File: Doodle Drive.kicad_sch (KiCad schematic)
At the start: 32 parts, among them J1 USB_B, J2 PINHD_1x4_Male, J6 PINHD_1x2_Male, SW1 Push_Button, SW2 Push_Button, SW3 Push_Button, U1 STM32F411RETx, U6 AP7343-30W5-7, Y1 32.768KHz ±20ppm 12.5pF, Y2 25MHZ 9PF

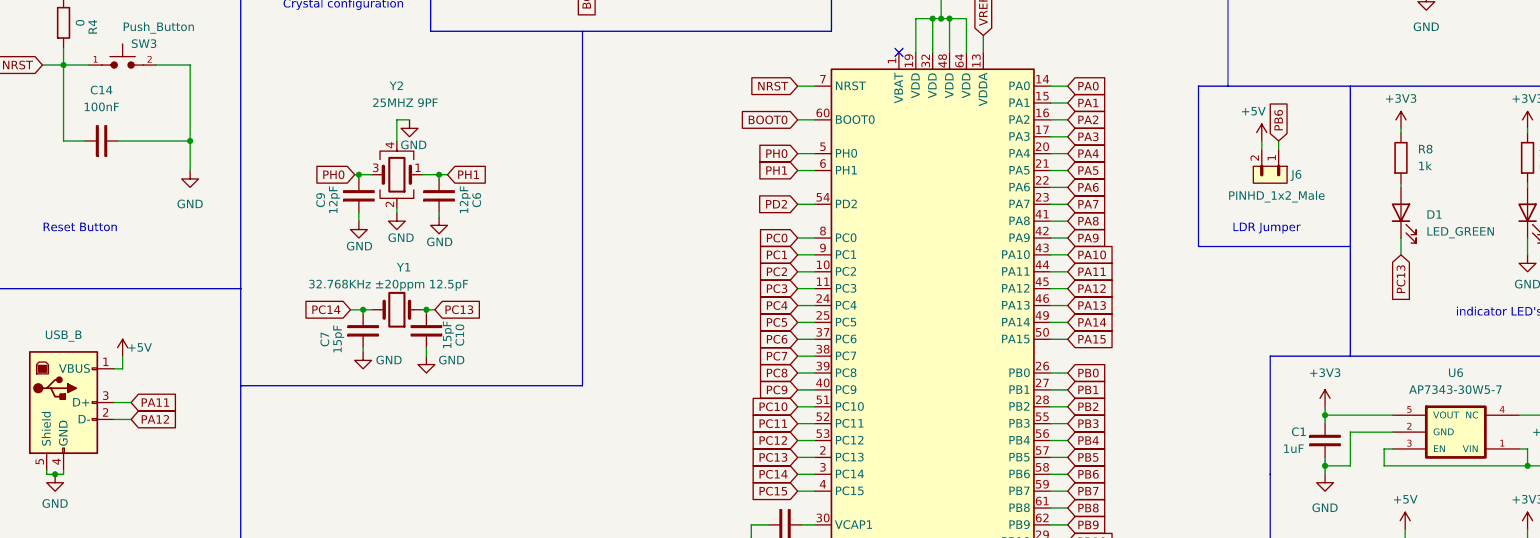
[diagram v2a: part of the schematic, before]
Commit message: fixed few errors, added test points
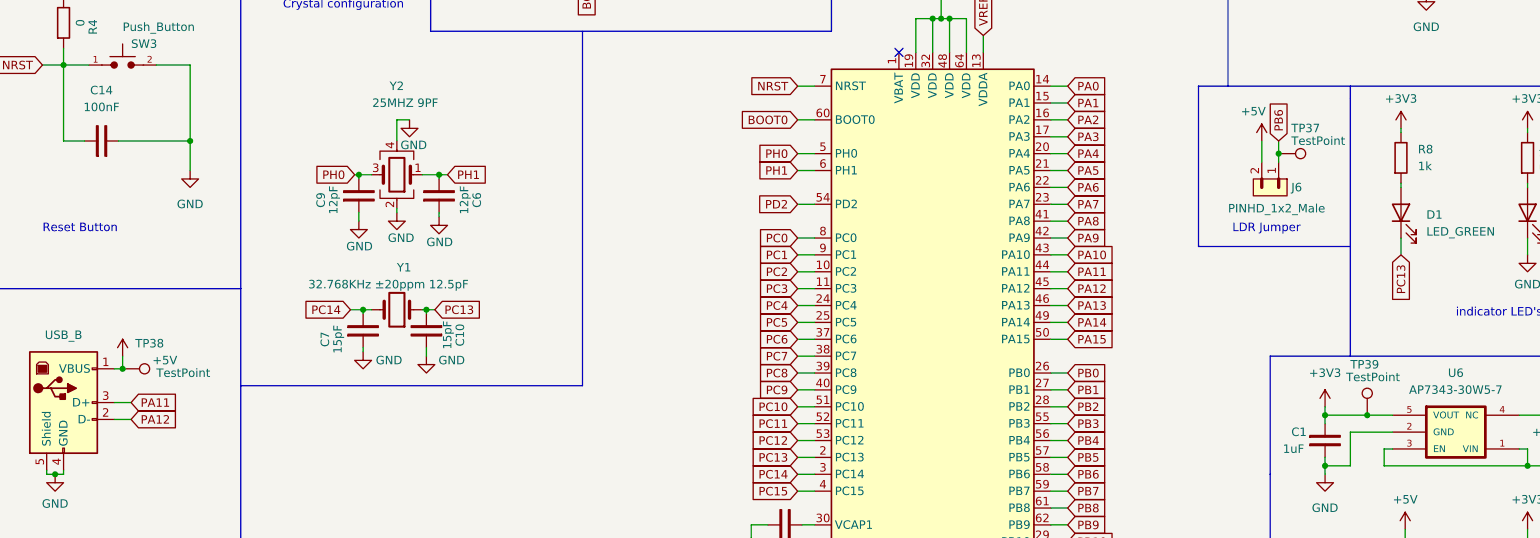
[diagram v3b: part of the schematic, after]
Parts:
- added TP37, TP38, TP39: TestPoint, TestPoint:TestPoint_Pad_D2.5mm, symbol Connector:TestPoint
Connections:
- net +3V3: now also TP39.1
- net +5V: now also TP38.1
- net PB6: now also TP37.1
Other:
- moved on the sheet: J6
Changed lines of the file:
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@@
   (junction (at 227.33 134.62) (diameter 0) (color 0 0 0 0)
   )
+  (junction (at 233.68 127) (diameter 0) (color 0 0 0 0)
+  )
   (junction (at 269.24 50.8) (diameter 0) (color 0 0 0 0)
   )
   (junction (at 36.195 135.89) (diameter 0) (color 0 0 0 0)
   )
+  (junction (at 46.355 120.015) (diameter 0) (color 0 0 0 0)
+  )
   (junction (at 56.515 85.725) (diameter 0) (color 0 0 0 0)
   )
@@
   )
   (junction (at 170.815 67.31) (diameter 0) (color 0 0 0 0)
+  )
+  (junction (at 220.345 87.63) (diameter 0) (color 0 0 0 0)
   )
   (junction (at 255.27 60.96) (diameter 0) (color 0 0 0 0)
@@
     (stroke (width 0) (type default))
   )
-  (wire (pts (xy 220.345 86.995) (xy 220.345 85.725))
+  (wire (pts (xy 220.345 88.9) (xy 220.345 87.63))
     (stroke (width 0) (type default))
   )
@@
     (stroke (width 0) (type default))
   )
+  (wire (pts (xy 233.68 127) (xy 237.49 127))
+    (stroke (width 0) (type default))
+  )
   (wire (pts (xy 256.54 132.08) (xy 257.81 132.08))
     (stroke (width 0) (type default))
@@
     (stroke (width 0) (type default))
   )
-  (wire (pts (xy 227.33 127) (xy 237.49 127))
+  (wire (pts (xy 227.33 127) (xy 233.68 127))
     (stroke (width 0) (type default))
   )
@@
     (stroke (width 0) (type default))
   )
-  (wire (pts (xy 217.805 86.995) (xy 217.805 85.725))
+  (wire (pts (xy 217.805 88.9) (xy 217.805 85.725))
     (stroke (width 0) (type default))
   )
@@
   )
   (wire (pts (xy 168.275 67.31) (xy 168.275 72.39))
+    (stroke (width 0) (type default))
+  )
+  (wire (pts (xy 220.345 87.63) (xy 220.345 85.725))
     (stroke (width 0) (type default))
   )
@@
     )
   )
+  (symbol (lib_id "Connector:TestPoint") (at 233.68 127 0) (unit 1)
+    (in_bom yes) (on_board yes) (dnp no)
+    (property "Reference" "TP39" (at 231.14 119.38 0)
+      (effects (font (size 1.27 1.27)) (justify left))
+    )
+    (property "Value" "TestPoint" (at 230.505 121.285 0)
+      (effects (font (size 1.27 1.27)) (justify left))
+    )
+    (property "Footprint" "TestPoint:TestPoint_Pad_D2.5mm" (at 238.76 127 0)
+      (effects (font (size 1.27 1.27)) hide)
+    )
+    (property "Datasheet" "~" (at 238.76 127 0)
+      (effects (font (size 1.27 1.27)) hide)
+    )
+    (pin "1")
+    (instances
+      (project "Doodle Drive"
+        (path "/3ec634aa-8c09-482d-9325-2288a4dbd68b"
+          (reference "TP39") (unit 1)
+        )
+      )
+    )
+  )
   (symbol (lib_id "PCM_SL_Devices:Capacitor_NP") (at 229.87 55.88 90) (unit 1)
     (in_bom yes) (on_board yes) (dnp no) (fields_autoplaced)
@@
     )
   )
-  (symbol (lib_id "PCM_SL_Pin_Headers:PINHD_1x2_Male") (at 219.075 90.805 270) (unit 1)
+  (symbol (lib_id "PCM_SL_Pin_Headers:PINHD_1x2_Male") (at 219.075 92.71 270) (unit 1)
     (in_bom yes) (on_board yes) (dnp no)
-    (property "Reference" "J6" (at 222.25 90.805 90)
+    (property "Reference" "J6" (at 222.25 92.71 90)
       (effects (font (size 1.27 1.27)) (justify left))
     )
-    (property "Value" "PINHD_1x2_Male" (at 212.725 93.98 90)
+    (property "Value" "PINHD_1x2_Male" (at 212.725 95.885 90)
       (effects (font (size 1.27 1.27)) (justify left))
     )
-    (property "Footprint" "Connector_PinHeader_2.54mm:PinHeader_1x02_P2.54mm_Vertical" (at 215.265 92.075 0)
-      (effects (font (size 1.27 1.27)) hide)
-    )
-    (property "Datasheet" "" (at 226.695 90.805 0)
+    (property "Footprint" "Connector_PinHeader_2.54mm:PinHeader_1x02_P2.54mm_Vertical" (at 215.265 93.98 0)
+      (effects (font (size 1.27 1.27)) hide)
+    )
+    (property "Datasheet" "" (at 226.695 92.71 0)
       (effects (font (size 1.27 1.27)) hide)
     )
@@
       (effects (font (size 1.27 1.27)) hide)
     )
-    (property "Value" "+5V" (at 48.895 116.84 0)
+    (property "Value" "+5V" (at 52.705 118.745 0)
       (effects (font (size 1.27 1.27)))
     )
@@
     )
   )
+  (symbol (lib_id "Connector:TestPoint") (at 46.355 120.015 270) (unit 1)
+    (in_bom yes) (on_board yes) (dnp no)
+    (property "Reference" "TP38" (at 48.26 116.205 90)
+      (effects (font (size 1.27 1.27)) (justify left))
+    )
+    (property "Value" "TestPoint" (at 51.435 120.65 90)
+      (effects (font (size 1.27 1.27)) (justify left))
+    )
+    (property "Footprint" "TestPoint:TestPoint_Pad_D2.5mm" (at 46.355 125.095 0)
+      (effects (font (size 1.27 1.27)) hide)
+    )
+    (property "Datasheet" "~" (at 46.355 125.095 0)
+      (effects (font (size 1.27 1.27)) hide)
+    )
+    (pin "1")
+    (instances
+      (project "Doodle Drive"
+        (path "/3ec634aa-8c09-482d-9325-2288a4dbd68b"
+          (reference "TP38") (unit 1)
+        )
+      )
+    )
+  )
   (symbol (lib_id "power:+5V") (at 261.62 133.35 0) (unit 1)
     (in_bom yes) (on_board yes) (dnp no)
@@
         )
       )
+    )
+  )
+  (symbol (lib_id "Connector:TestPoint") (at 220.345 87.63 270) (unit 1)
+    (in_bom yes) (on_board yes) (dnp no)
+    (property "Reference" "TP37" (at 222.25 83.82 90)
+      (effects (font (size 1.27 1.27)) (justify left))
+    )
+    (property "Value" "TestPoint" (at 222.25 85.725 90)
+      (effects (font (size 1.27 1.27)) (justify left))
+    )
+    (property "Footprint" "TestPoint:TestPoint_Pad_D2.5mm" (at 220.345 92.71 0)
+      (effects (font (size 1.27 1.27)) hide)
+    )
+    (property "Datasheet" "~" (at 220.345 92.71 0)
+      (effects (font (size 1.27 1.27)) hide)
+    )
+    (pin "1")
+    (instances
+      (project "Doodle Drive"
+        (path "/3ec634aa-8c09-482d-9325-2288a4dbd68b"
+          (reference "TP37") (unit 1)
+        )
+      )

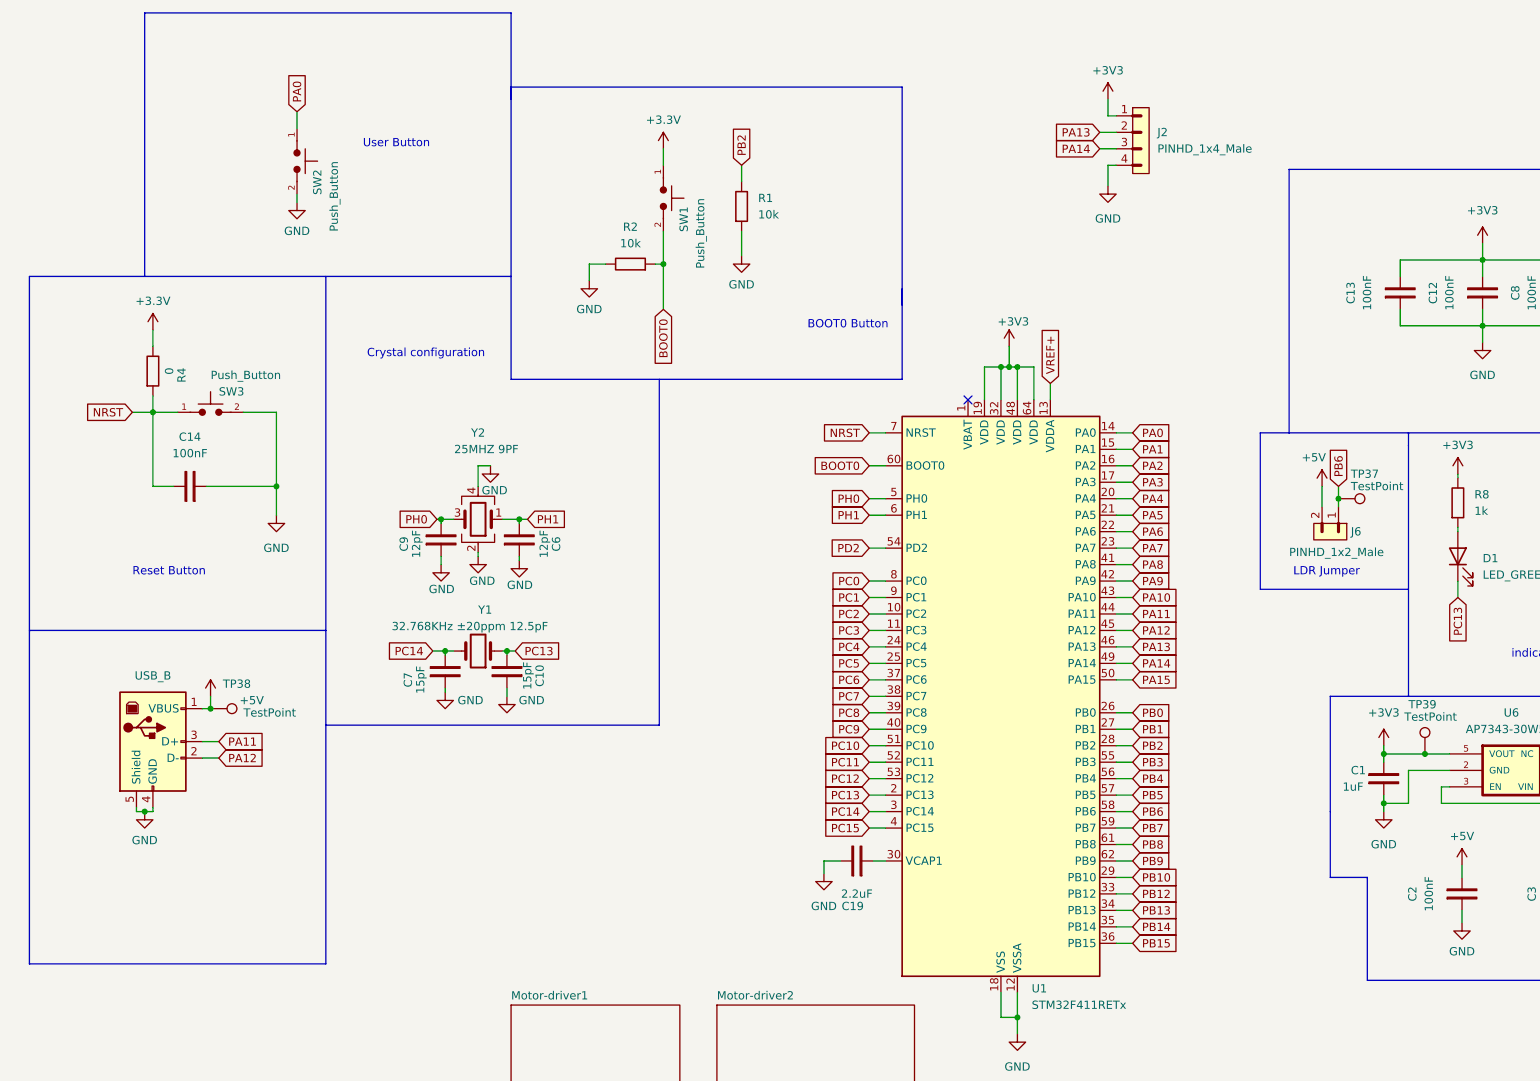
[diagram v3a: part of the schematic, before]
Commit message: add CP2102 USB to UART chip
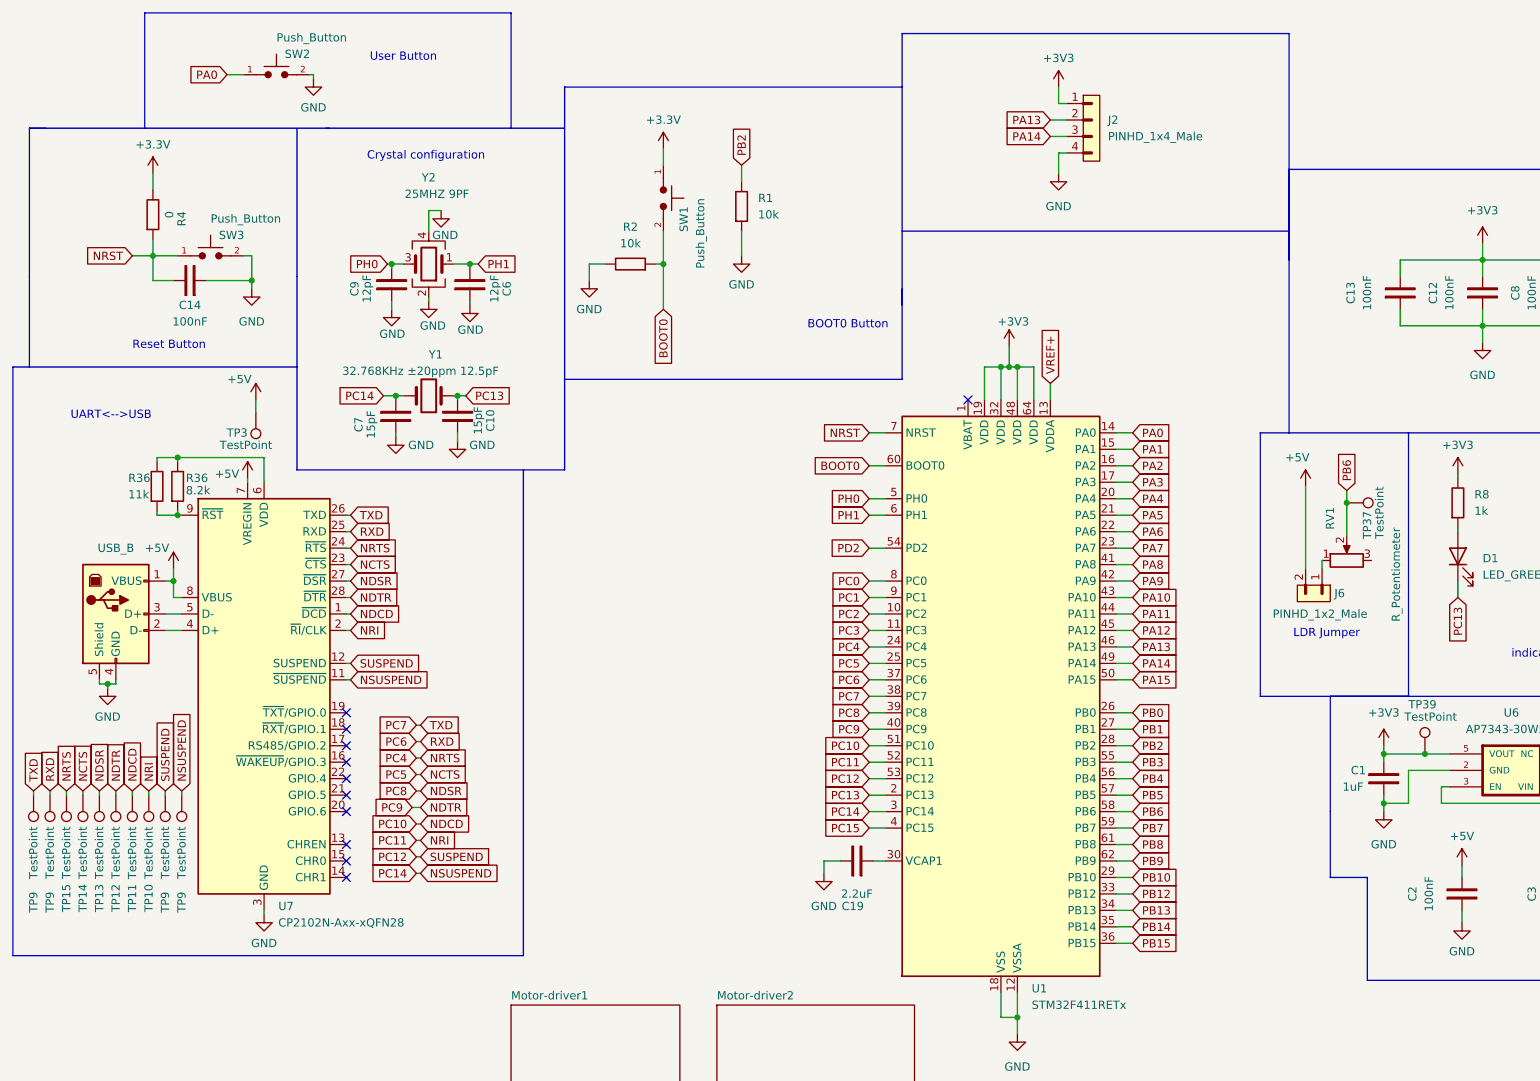
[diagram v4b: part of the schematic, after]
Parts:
- removed TP38: TestPoint, TestPoint:TestPoint_Pad_D2.5mm, symbol Connector:TestPoint
- added R36: 11k, Resistor_SMD:R_0805_2012Metric, symbol PCM_SL_Devices:Resistor
- added R36: 8.2k, Resistor_SMD:R_0805_2012Metric, symbol PCM_SL_Devices:Resistor
- added RV1: R_Potentiometer, Potentiometer_THT:Potentiometer_ACP_CA6-H2,5_Horizontal, symbol Device:R_Potentiometer
- added TP10, TP11, TP12, TP13, TP14, TP15, TP3, TP9 (x4): TestPoint, TestPoint:TestPoint_Pad_D2.5mm, symbol Connector:TestPoint
- added U7: CP2102N-Axx-xQFN28, Package_DFN_QFN:QFN-28-1EP_5x5mm_P0.5mm_EP3.35x3.35mm, symbol Interface_USB:CP2102N-Axx-xQFN28
- C1: footprint (none) -> Capacitor_SMD:C_0805_2012Metric
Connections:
- net +5V: now also TP3.1, U7.7 (VREGIN), U7.8 (VBUS)
- net GND: now also U7.29 (GND), U7.3 (GND)
- net PA11: no longer J1.3 (D+)
- net PA12: no longer J1.2 (D-)
- net PB6: now also RV1.2; no longer J6.1
- net PC12: now also TP9.1, U7.12 (SUSPEND)
- net PC6: now also TP9.1, U7.25 (RXD)
- net PC7: now also TP9.1, U7.26 (TXD)
- net PC10 renamed NDCD
- net NDCD: now also TP11.1, U7.1 (~{DCD})
- net PC11 renamed NRI
- net NRI: now also TP10.1, U7.2 (~{RI}/CLK)
- net PC14 renamed NSUSPEND
- net NSUSPEND: now also TP9.1, U7.11 (~{SUSPEND})
- net PC4 renamed NRTS
- net NRTS: now also TP15.1, U7.24 (~{RTS})
- net PC5 renamed NCTS
- net NCTS: now also TP14.1, U7.23 (~{CTS})
- net PC8 renamed NDSR
- net NDSR: now also TP13.1, U7.27 (~{DSR})
- net PC9 renamed NDTR
- net NDTR: now also TP12.1, U7.28 (~{DTR})
- new net: J6.1, RV1.1
- new net: R36.1, R36.1, U7.9 (~{RST})
- new net: R36.2, R36.2, U7.6 (VDD)
- new net: J1.2 (D-), U7.4 (D+)
- new net: J1.3 (D+), U7.5 (D-)
- no-connect marks 1 -> 11
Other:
- note added: "UART<-->USB"
- moved on the sheet: C10, C14, C6, C7, C9, J2, J6, R4, SW2, SW3, TP37, Y1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
